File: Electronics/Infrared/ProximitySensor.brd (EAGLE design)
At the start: 45.2 x 16.8 mm, 9 parts, among them IC1 LM358D

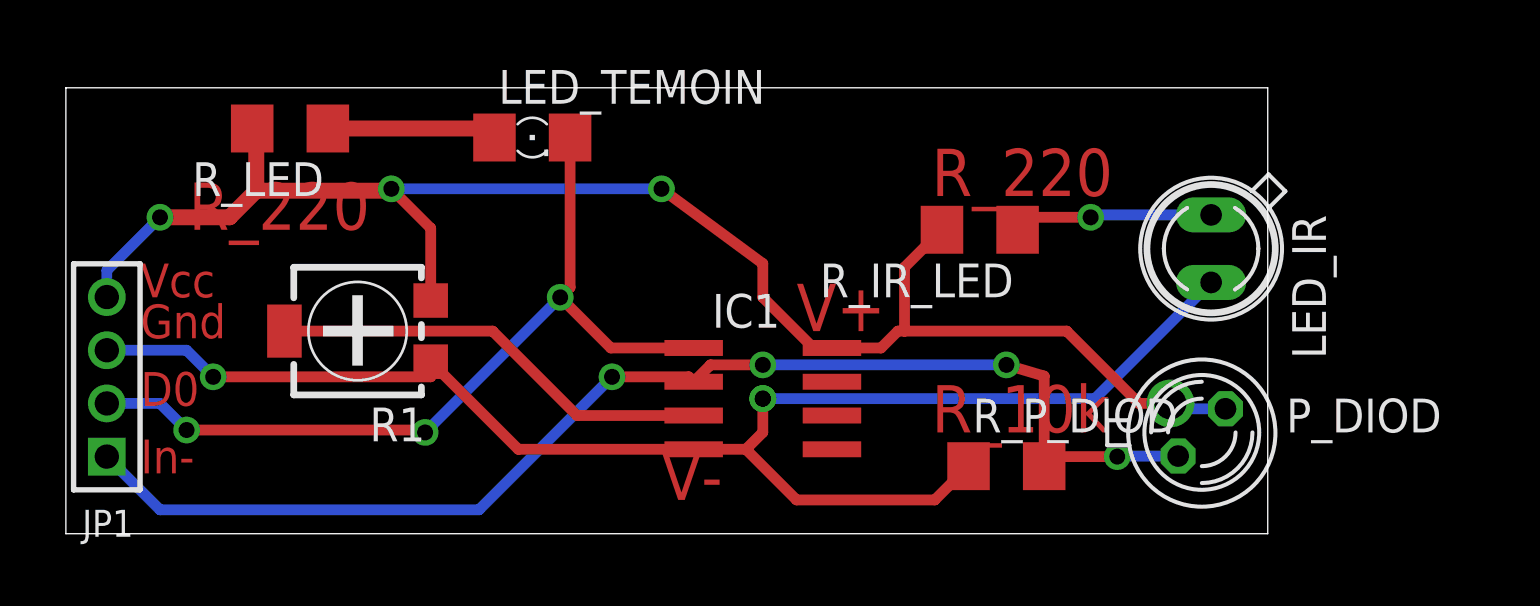
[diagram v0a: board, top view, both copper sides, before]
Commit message: modification de la carte (trimmer CMS en trimmer THT)
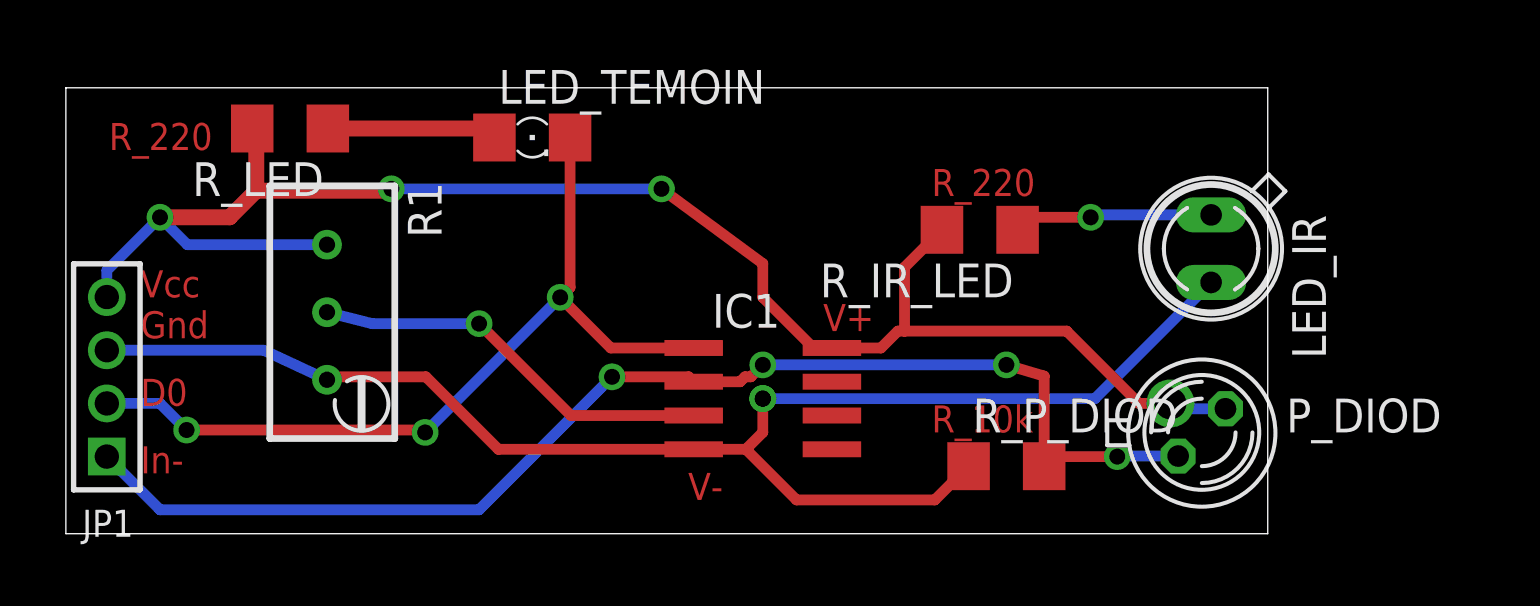
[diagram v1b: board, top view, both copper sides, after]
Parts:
- R1: device rcl:RTRIM4G/J -> rcl:RTRIMT93YA
- moved R1 1.35 mm to (10.3, 46.4), turned to 180 degrees
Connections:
- net GND: now also R1.3; no longer R1.1
- net VCC: now also R1.1; no longer R1.3
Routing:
- net VCC: track 60.6 -> 62.3 mm
- net N$2: track 16.7 -> 15.3 mm, vias 0 -> 1
- net GND: track 56.9 -> 56.0 mm, vias 2 -> 1
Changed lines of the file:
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@@
 <wire x1="45.66" y1="54.87" x2="0.46" y2="54.87" width="0" layer="20"/>
 <wire x1="0.46" y1="54.87" x2="0.46" y2="38.1" width="0" layer="20"/>
-<text x="3.27" y="46.99" size="1.27" layer="1">Vcc</text>
-<text x="3.27" y="45.45" size="1.27" layer="1">Gnd</text>
-<text x="3.27" y="42.91" size="1.27" layer="1">D0</text>
-<text x="3.27" y="40.37" size="1.27" layer="1">In-</text>
-<text x="27.94" y="45.72" size="1.778" layer="1">V+</text>
-<text x="22.86" y="39.37" size="1.778" layer="1">V-</text>
-<text x="33.02" y="50.8" size="1.778" layer="1">R_220</text>
-<text x="33.02" y="41.91" size="1.778" layer="1">R_10k</text>
-<text x="5.08" y="49.53" size="1.778" layer="1">R_220</text>
+<text x="3.27" y="46.99" size="1.016" layer="1">Vcc</text>
+<text x="3.27" y="45.45" size="1.016" layer="1">Gnd</text>
+<text x="3.27" y="42.91" size="1.016" layer="1">D0</text>
+<text x="3.27" y="40.37" size="1.016" layer="1">In-</text>
+<text x="28.94" y="45.72" size="1.016" layer="1">V+</text>
+<text x="23.86" y="39.37" size="1.016" layer="1">V-</text>
+<text x="33.02" y="50.8" size="1.016" layer="1">R_220</text>
+<text x="33.02" y="41.91" size="1.016" layer="1">R_10k</text>
+<text x="2.08" y="52.53" size="1.016" layer="1">R_220</text>
 </plain>
 <attributes>
@@
 </element>
 <element name="IC1" library="linear" package="SO08" value="LM358D" x="26.67" y="43.18" rot="R270"/>
-<element name="R1" library="rcl" package="RTRIM4G/J" value="" x="11.43" y="45.72" rot="R90"/>
+<element name="R1" library="rcl" package="RTRIMT93YA" value="" x="10.28" y="46.43" rot="R180"/>
 <element name="R_IR_LED" library="eagle-ltspice" package="R1206" value="" x="34.83" y="49.53" rot="R180">
 <attribute name="SPICEMODEL" value="NONE" x="34.83" y="49.53" size="1.778" layer="27" rot="R180" display="off"/>
@@
 <signals>
 <signal name="VCC">
-<contactref element="R1" pad="3"/>
+<contactref element="R1" pad="1"/>
 <contactref element="R_IR_LED" pad="2"/>
 <contactref element="R_LED" pad="2"/>
 <contactref element="P_DIOD" pad="K"/>
 <contactref element="IC1" pad="8"/>
-<wire x1="14.18" y1="46.87" x2="14.06" y2="46.99" width="0.4064" layer="1"/>
 <via x="12.7" y="51.07" extent="1-16" drill="0.6" shape="square"/>
 <via x="22.86" y="51.07" extent="1-16" drill="0.6" shape="square"/>
@@
 <wire x1="12.7" y1="51.07" x2="12.63" y2="51" width="0.4064" layer="1"/>
 <wire x1="12.63" y1="51" x2="7.62" y2="51" width="0.6" layer="1"/>
-<wire x1="12.7" y1="51.07" x2="14.18" y2="49.59" width="0.4064" layer="1"/>
-<wire x1="14.18" y1="49.59" x2="14.18" y2="46.87" width="0.4064" layer="1"/>
 <via x="42" y="43" extent="1-16" drill="1.2" shape="square"/>
 <wire x1="44.069" y1="42.799" x2="42.201" y2="42.799" width="0.4064" layer="16"/>
@@
 <wire x1="42" y1="43" x2="40.82" y2="43" width="0.4064" layer="1"/>
 <wire x1="40.82" y1="43" x2="38.1" y2="45.72" width="0.4064" layer="1"/>
+<wire x1="10.28" y1="48.97" x2="5.03" y2="48.97" width="0.4064" layer="16"/>
+<wire x1="5.03" y1="48.97" x2="4" y2="50" width="0.4064" layer="16"/>
 </signal>
 <signal name="GND">
-<contactref element="R1" pad="1"/>
+<contactref element="R1" pad="3"/>
 <contactref element="LED_IR" pad="K"/>
 <contactref element="R_P_DIOD" pad="1"/>
 <contactref element="IC1" pad="4"/>
-<wire x1="24.07" y1="41.275" x2="17.475" y2="41.275" width="0.4064" layer="1"/>
-<wire x1="17.475" y1="41.275" x2="14.18" y2="44.57" width="0.4064" layer="1"/>
+<wire x1="24.07" y1="41.275" x2="16.725" y2="41.275" width="0.4064" layer="1"/>
 <wire x1="24.07" y1="41.275" x2="26.035" y2="41.275" width="0.4064" layer="1"/>
 <wire x1="26.035" y1="41.275" x2="27.94" y2="39.37" width="0.4064" layer="1"/>
@@
 <contactref element="JP1" pad="3"/>
 <wire x1="43.53" y1="47.55" x2="39.16" y2="43.18" width="0.4064" layer="16"/>
-<wire x1="14.18" y1="44.57" x2="14.18" y2="44" width="0.4064" layer="1"/>
-<wire x1="14.18" y1="44" x2="6" y2="44" width="0.4064" layer="1"/>
-<via x="6" y="44" extent="1-16" drill="0.6" shape="square"/>
-<wire x1="6" y1="44" x2="5" y2="45" width="0.4064" layer="16"/>
-<wire x1="5" y1="45" x2="2" y2="45" width="0.4064" layer="16"/>
+<wire x1="16.725" y1="41.275" x2="14" y2="44" width="0.4064" layer="1"/>
+<wire x1="2" y1="45" x2="7.9" y2="45" width="0.4064" layer="16"/>
+<wire x1="7.9" y1="45" x2="10.28" y2="43.89" width="0.4064" layer="16"/>
+<wire x1="14" y1="44" x2="10.28" y2="44" width="0.4064" layer="1"/>
+<wire x1="10.28" y1="44" x2="10.28" y2="43.89" width="0.4064" layer="1"/>
 </signal>
 <signal name="D0">
@@
 <contactref element="R1" pad="2"/>
 <contactref element="IC1" pad="3"/>
-<wire x1="8.68" y1="45.72" x2="16.51" y2="45.72" width="0.4064" layer="1"/>
-<wire x1="16.51" y1="45.72" x2="19.685" y2="42.545" width="0.4064" layer="1"/>
-<wire x1="19.685" y1="42.545" x2="24.07" y2="42.545" width="0.4064" layer="1"/>
+<wire x1="19.455" y1="42.545" x2="24.07" y2="42.545" width="0.4064" layer="1"/>
+<wire x1="19.455" y1="42.545" x2="16" y2="46" width="0.4064" layer="1"/>
+<via x="16" y="46" extent="1-16" drill="0.6" shape="square"/>
+<wire x1="16" y1="46" x2="11.98" y2="46" width="0.4064" layer="16"/>
+<wire x1="11.98" y1="46" x2="10.28" y2="46.43" width="0.4064" layer="16"/>
 </signal>
 <signal name="IN-">
@@
 <wire x1="35.83" y1="44.45" x2="26.67" y2="44.45" width="0.4064" layer="16"/>
 <via x="26.67" y="44.45" extent="1-16" drill="0.6" shape="square"/>
-<wire x1="26.67" y1="44.45" x2="24.705" y2="44.45" width="0.4064" layer="1"/>
-<wire x1="24.705" y1="44.45" x2="24.07" y2="43.815" width="0.4064" layer="1"/>
 <contactref element="JP1" pad="1"/>
 <wire x1="37.252" y1="40.64" x2="37.612" y2="41" width="0.4064" layer="1"/>
@@
 <wire x1="16" y1="39" x2="4" y2="39" width="0.4064" layer="16"/>
 <wire x1="4" y1="39" x2="2" y2="41" width="0.4064" layer="16"/>
+<wire x1="24.07" y1="43.815" x2="25.815" y2="43.815" width="0.4064" layer="1"/>
+<wire x1="25.815" y1="43.815" x2="26" y2="44" width="0.4064" layer="1"/>
+<wire x1="26" y1="44" x2="26.22" y2="44" width="0.4064" layer="1"/>
+<wire x1="26.22" y1="44" x2="26.67" y2="44.45" width="0.4064" layer="1"/>
 </signal>
 <signal name="N$1">
